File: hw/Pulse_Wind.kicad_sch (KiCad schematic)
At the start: 21 parts, among them J1 AudioJack4, J2 Conn_01x04, U1 PY32F003F18U6, U2 SC7A20, U3 FM8002A, U9 ME6206A33XG

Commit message: hw: Layout & routing
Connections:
- net +3V3: now also J2.1 (Pin_1)
- net VIN: no longer J2.1 (Pin_1)
- net at C4.2, R5.2, U3.5 (VO1): now also LS1.1; no longer LS1.2
- net at U3.8 (VO2): now also LS1.2; no longer LS1.1
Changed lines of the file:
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@@
 	(symbol
 		(lib_id "Device:Speaker")
-		(at 245.11 105.41 0)
-		(unit 1)
-		(exclude_from_sim no)
-		(in_bom yes)
-		(on_board yes)
-		(dnp no)
-		(fields_autoplaced yes)
+		(at 245.11 107.95 0)
+		(mirror x)
+		(unit 1)
+		(exclude_from_sim no)
+		(in_bom yes)
+		(on_board yes)
+		(dnp no)
 		(property "Reference" "LS1"
-			(at 250.19 105.4099 0)
+			(at 250.19 105.41 0)
 			(effects
 				(font
@@
 		)
 		(property "Value" "Speaker"
-			(at 250.19 107.9499 0)
+			(at 250.19 107.95 0)
 			(effects
 				(font
@@
 		)
 		(property "Footprint" "Pulse_footprints:Pads_P2.00"
-			(at 245.11 110.49 0)
+			(at 245.11 102.87 0)
 			(effects
 				(font
@@
 		)
 		(property "Description" "Speaker"
-			(at 245.11 105.41 0)
+			(at 245.11 107.95 0)
 			(effects
 				(font
@@
 			)
 		)
-		(property "Value" "VIN"
-			(at 92.456 88.9 90)
-			(effects
-				(font
+		(property "Value" "+3V3"
+			(at 93.472 88.646 90)
+			(effects
+				(font

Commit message: hw: Adjust silkscreen
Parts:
- renumbered C91 to C7, C92 to C8, U9 to U4
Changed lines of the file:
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@@
 		(on_board yes)
 		(dnp no)
-		(property "Reference" "C91"
+		(property "Reference" "C7"
 			(at 34.798 71.12 0)
 			(effects
@@
 			(project "Pulse_Wind"
 				(path "/49429a57-8612-48d8-83b1-7633b6997710"
-					(reference "C91")
+					(reference "C7")
 					(unit 1)
 				)
@@
 		(on_board yes)
 		(dnp no)
-		(property "Reference" "C92"
+		(property "Reference" "C8"
 			(at 62.738 71.12 0)
 			(effects
@@
 			(project "Pulse_Wind"
 				(path "/49429a57-8612-48d8-83b1-7633b6997710"
-					(reference "C92")
+					(reference "C8")
 					(unit 1)
 				)
@@
 		(dnp no)
 		(fields_autoplaced yes)
-		(property "Reference" "U9"
+		(property "Reference" "U4"
 			(at 52.07 62.23 0)
 			(effects
@@
 			(project "Pulse_Wind"
 				(path "/49429a57-8612-48d8-83b1-7633b6997710"
-					(reference "U9")
-					(unit 1)
-				)
+					(reference "U4")
+					(unit 1)
+				)

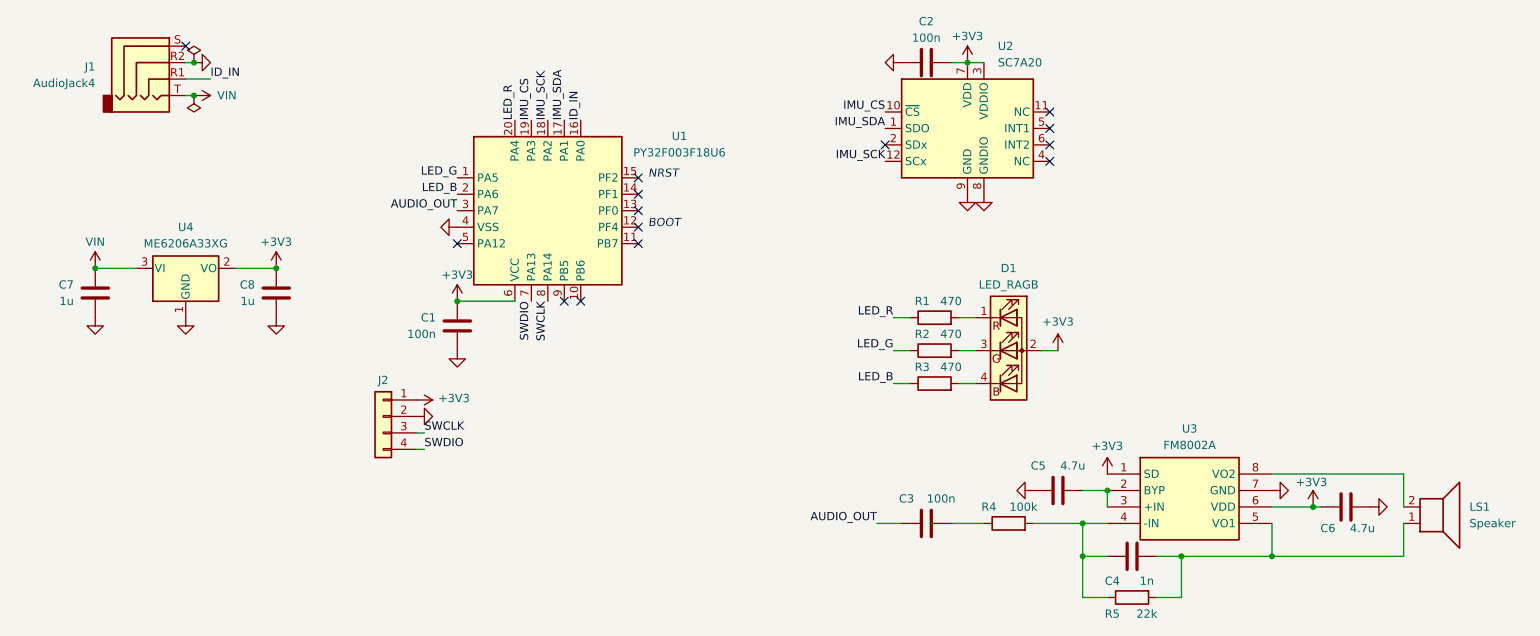
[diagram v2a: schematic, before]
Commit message: hw: Fix errors (> <)
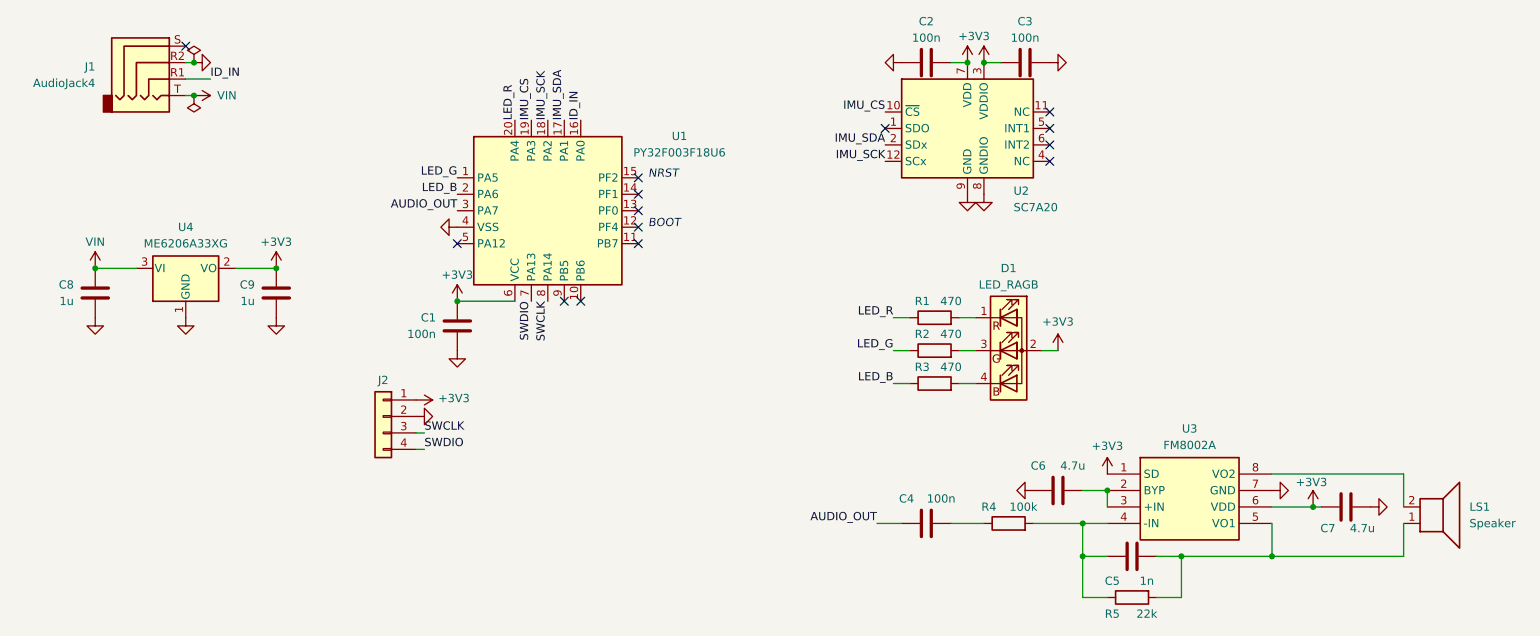
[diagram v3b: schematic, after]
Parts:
- added C3: 100n, Capacitor_SMD:C_0402_1005Metric, symbol Device:C
- renumbered C3 to C4, C4 to C5, C5 to C6, C6 to C7, C7 to C8, C8 to C9
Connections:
- net +3V3: now also C3.1
- net GND: now also C3.2
- net IMU_SDA: now also U2.2 (SDx); no longer U2.1 (SDO)
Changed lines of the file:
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@@
 	)
 	(junction
+		(at 175.26 36.83)
+		(diameter 0)
+		(color 0 0 0 0)
+	)
+	(junction
 		(at 205.74 113.03)
 		(diameter 0)
@@
 	)
 	(no_connect
-		(at 160.02 49.53)
-	)
-	(no_connect
 		(at 185.42 49.53)
 	)
@@
 		(at 185.42 44.45)
 	)
+	(no_connect
+		(at 160.02 46.99)
+	)
 	(wire
 		(pts
@@
 	(wire
 		(pts
-			(xy 172.72 36.83) (xy 175.26 36.83)
-		)
-		(stroke
-			(width 0)
-			(type default)
-		)
-	)
-	(wire
-		(pts
 			(xy 219.71 105.41) (xy 226.06 105.41)
 		)
@@
 	(wire
 		(pts
+			(xy 177.8 36.83) (xy 175.26 36.83)
+		)
+		(stroke
+			(width 0)
+			(type default)
+		)
+	)
+	(wire
+		(pts
 			(xy 190.5 113.03) (xy 194.31 113.03)
 		)
@@
 	)
 	(label "IMU_SDA"
-		(at 160.02 46.99 180)
+		(at 160.02 49.53 180)
 		(effects
 			(font
@@
 	)
 	(symbol
+		(lib_id "Device:C")
+		(at 181.61 36.83 90)
+		(unit 1)
+		(exclude_from_sim no)
+		(in_bom yes)
+		(on_board yes)
+		(dnp no)
+		(property "Reference" "C3"
+			(at 181.61 30.48 90)
+			(effects
+				(font
+					(size 1.27 1.27)
+				)
+			)
+		)
+		(property "Value" "100n"
+			(at 181.61 33.02 90)
+			(effects
+				(font
+					(size 1.27 1.27)
+				)
+			)
+		)
+		(property "Footprint" "Capacitor_SMD:C_0402_1005Metric"
+			(at 185.42 35.8648 0)
+			(effects
+				(font
+					(size 1.27 1.27)
+				)
+				(hide yes)
+			)
+		)
+		(property "Datasheet" "~"
+			(at 181.61 36.83 0)
+			(effects
+				(font
+					(size 1.27 1.27)
+				)
+				(hide yes)
+			)
+		)
+		(property "Description" "Unpolarized capacitor"
+			(at 181.61 36.83 0)
+			(effects
+				(font
+					(size 1.27 1.27)
+				)
+				(hide yes)
+			)
+		)
+		(pin "1"
+		)
+		(pin "2"
+		)
+		(instances
+			(project "Pulse_Wind"
+				(path "/49429a57-8612-48d8-83b1-7633b6997710"
+					(reference "C3")
+					(unit 1)
+				)
+			)
+		)
+	)
+	(symbol
 		(lib_id "Device:R")
 		(at 167.64 76.2 90)
@@
 		(on_board yes)
 		(dnp no)
-		(property "Reference" "C7"
+		(property "Reference" "C8"
 			(at 34.798 71.12 0)
 			(effects
@@
 			(project "Pulse_Wind"
 				(path "/49429a57-8612-48d8-83b1-7633b6997710"
-					(reference "C7")
+					(reference "C8")
 					(unit 1)
 				)
@@
 	)
 	(symbol
+		(lib_id "power:GND")
+		(at 185.42 36.83 90)
+		(unit 1)
+		(exclude_from_sim no)
+		(in_bom yes)
+		(on_board yes)
+		(dnp no)
+		(fields_autoplaced yes)
+		(property "Reference" "#PWR031"
+			(at 191.77 36.83 0)
+			(effects
+				(font
+					(size 1.27 1.27)
+				)
+				(hide yes)
+			)
+		)
+		(property "Value" "GND"
+			(at 190.5 36.83 0)
+			(effects
+				(font
+					(size 1.27 1.27)
+				)
+				(hide yes)
+			)
+		)
+		(property "Footprint" ""
+			(at 185.42 36.83 0)
+			(effects
+				(font
+					(size 1.27 1.27)
+				)
+				(hide yes)
+			)
+		)
+		(property "Datasheet" ""
+			(at 185.42 36.83 0)
+			(effects
+				(font
+					(size 1.27 1.27)
+				)
+				(hide yes)
+			)
+		)
+		(property "Description" "Power symbol creates a global label with name \"GND\" , ground"
+			(at 185.42 36.83 0)
+			(effects
+				(font
+					(size 1.27 1.27)
+				)
+				(hide yes)
+			)
+		)
+		(pin "1"
+		)
+		(instances
+			(project "Pulse_Wind"
+				(path "/49429a57-8612-48d8-83b1-7633b6997710"
+					(reference "#PWR031")
+					(unit 1)
+				)
+			)
+		)
+	)
+	(symbol
 		(lib_id "Device:C")
 		(at 166.37 107.95 90)
@@
 		(on_board yes)
 		(dnp no)
-		(property "Reference" "C3"
+		(property "Reference" "C4"
 			(at 163.322 104.14 90)
 			(effects
@@
 			(project ""
 				(path "/49429a57-8612-48d8-83b1-7633b6997710"
-					(reference "C3")
+					(reference "C4")
 					(unit 1)
 				)
@@
 		(on_board yes)
 		(dnp no)
-		(property "Reference" "C8"
+		(property "Reference" "C9"
 			(at 62.738 71.12 0)
 			(effects
@@
 			(project "Pulse_Wind"
 				(path "/49429a57-8612-48d8-83b1-7633b6997710"
-					(reference "C8")
+					(reference "C9")
 					(unit 1)
 				)
@@
 		(on_board yes)
 		(dnp no)
-		(property "Reference" "C4"
+		(property "Reference" "C5"
 			(at 195.072 116.84 90)
 			(effects
@@
 			(project "Pulse_Wind"
 				(path "/49429a57-8612-48d8-83b1-7633b6997710"
-					(reference "C4")
+					(reference "C5")
 					(unit 1)
 				)
@@
 		(on_board yes)
 		(dnp no)
-		(property "Reference" "C5"
+		(property "Reference" "C6"
 			(at 183.642 99.06 90)
 			(effects
@@
 			(project "Pulse_Wind"
 				(path "/49429a57-8612-48d8-83b1-7633b6997710"
-					(reference "C5")
+					(reference "C6")
 					(unit 1)
 				)
@@
 		)
 		(property "Value" "+3V3"
-			(at 172.72 32.766 0)
+			(at 173.736 32.766 0)
 			(effects
 				(font
@@
 		(on_board yes)
 		(dnp no)
-		(fields_autoplaced yes)
 		(property "Reference" "U2"
-			(at 177.4033 34.29 0)
+			(at 179.832 56.642 0)
 			(effects
 				(font
@@
 		)
 		(property "Value" "SC7A20"
-			(at 177.4033 36.83 0)
+			(at 179.832 59.182 0)
 			(effects
 				(font
@@
 	)
 	(symbol
+		(lib_id "power:+3V3")
+		(at 175.26 36.83 0)
+		(unit 1)
+		(exclude_from_sim no)
+		(in_bom yes)
+		(on_board yes)
+		(dnp no)
+		(property "Reference" "#PWR05"
+			(at 175.26 40.64 0)
+			(effects
+				(font
+					(size 1.27 1.27)
+				)
+				(hide yes)
+			)
+		)
+		(property "Value" "+3V3"
+			(at 175.26 32.766 0)
+			(effects
+				(font
+					(size 1.27 1.27)
+				)
+				(hide yes)
+			)
+		)
+		(property "Footprint" ""
+			(at 175.26 36.83 0)
+			(effects
+				(font
+					(size 1.27 1.27)
+				)
+				(hide yes)
+			)
+		)
+		(property "Datasheet" ""
+			(at 175.26 36.83 0)
+			(effects
+				(font
+					(size 1.27 1.27)
+				)
+				(hide yes)
+			)
+		)
+		(property "Description" "Power symbol creates a global label with name \"+3V3\""
+			(at 175.26 36.83 0)
+			(effects
+				(font
+					(size 1.27 1.27)
+				)
+				(hide yes)
+			)
+		)
+		(pin "1"
+		)
+		(instances
+			(project "Pulse_Wind"
+				(path "/49429a57-8612-48d8-83b1-7633b6997710"
+					(reference "#PWR05")
+					(unit 1)
+				)
+			)
+		)
+	)
+	(symbol
 		(lib_id "Regulator_Linear:MCP1703Ax-330xxTT")
 		(at 52.07 68.58 0)
@@
 		(on_board yes)
 		(dnp no)
-		(property "Reference" "C6"
+		(property "Reference" "C7"
 			(at 228.346 108.712 90)
 			(effects
@@
 			(project "Pulse_Wind"
 				(path "/49429a57-8612-48d8-83b1-7633b6997710"
-					(reference "C6")
+					(reference "C7")
 					(unit 1)
 				)

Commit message: hw: Connect SC7A20 NC (pin 4) to GND?
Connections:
- net GND: now also U2.4 (NC)
- no-connect marks 14 -> 13
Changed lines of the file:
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@@
 	)
 	(no_connect
-		(at 185.42 52.07)
-	)
-	(no_connect
 		(at 110.49 73.66)
 	)
@@
 					(unit 1)
 				)
+			)
+		)
+	)
+	(symbol
+		(lib_id "power:GND")
+		(at 185.42 52.07 90)
+		(unit 1)
+		(exclude_from_sim no)
+		(in_bom yes)
+		(on_board yes)
+		(dnp no)
+		(fields_autoplaced yes)
+		(property "Reference" "#PWR032"
+			(at 191.77 52.07 0)
+			(effects
+				(font
+					(size 1.27 1.27)
+				)
+				(hide yes)
+			)
+		)
+		(property "Value" "GND"
+			(at 190.5 52.07 0)
+			(effects
+				(font
+					(size 1.27 1.27)
+				)
+				(hide yes)
+			)
+		)
+		(property "Footprint" ""
+			(at 185.42 52.07 0)
+			(effects
+				(font
+					(size 1.27 1.27)
+				)
+				(hide yes)
+			)
+		)
+		(property "Datasheet" ""
+			(at 185.42 52.07 0)
+			(effects
+				(font
+					(size 1.27 1.27)
+				)
+				(hide yes)
+			)
+		)
+		(property "Description" "Power symbol creates a global label with name \"GND\" , ground"
+			(at 185.42 52.07 0)
+			(effects
+				(font
+					(size 1.27 1.27)
+				)
+				(hide yes)
+			)
+		)
+		(pin "1"
+		)
+		(instances
+			(project "Pulse_Wind"
+				(path "/49429a57-8612-48d8-83b1-7633b6997710"
+					(reference "#PWR032")
+					(unit 1)
+				)

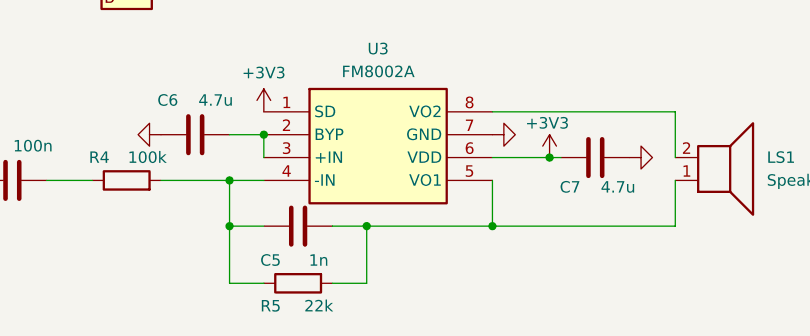
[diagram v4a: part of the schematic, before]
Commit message: hw: Comment schematic with actual components used
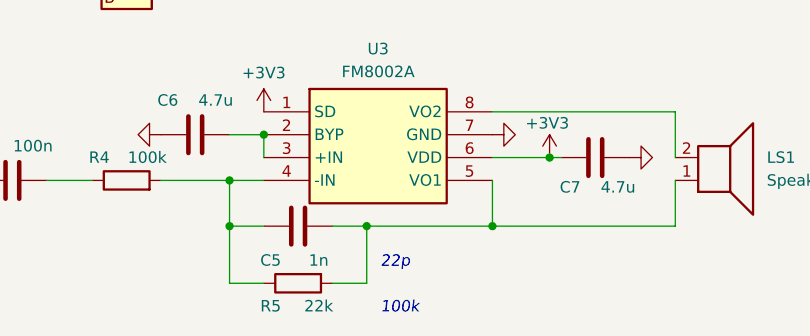
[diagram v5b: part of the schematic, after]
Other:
- note added: "100k"
- note added: "22p"
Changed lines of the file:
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@@
 	(generator_version "9.0")
 	(paper "A4")
+	(text "22p"
+		(exclude_from_sim no)
+		(at 207.264 117.094 0)
+		(effects
+			(font
+				(size 1.27 1.27)
+				(italic yes)
+			)
+			(justify left)
+		)
+	)
 	(text "NRST"
 		(exclude_from_sim no)
@@
 		(effects
 			(font
+				(size 1.27 1.27)
+				(italic yes)
+			)
+			(justify left)
+		)
+	)
+	(text "100k"
+		(exclude_from_sim no)
+		(at 207.264 122.174 0)
+		(effects
+			(font
